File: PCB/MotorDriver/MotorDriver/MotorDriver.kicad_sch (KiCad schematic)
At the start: 74 parts, among them J13 JST-XH, J14 JST-XH, J2 JST-XH, J3 XT30PW-M, J5 JST-XH, J6 JST-XH, J7 JST-XH, J8 JST-XH, J9 JST-XH, Q10 NMOS, Q3 TJ60S04M3L, SW1 SW_Push, SW2 SW_DPST_x2, U1 Pico, U15 AZ1117CH-3.3TR, U3 TCA9548APWR

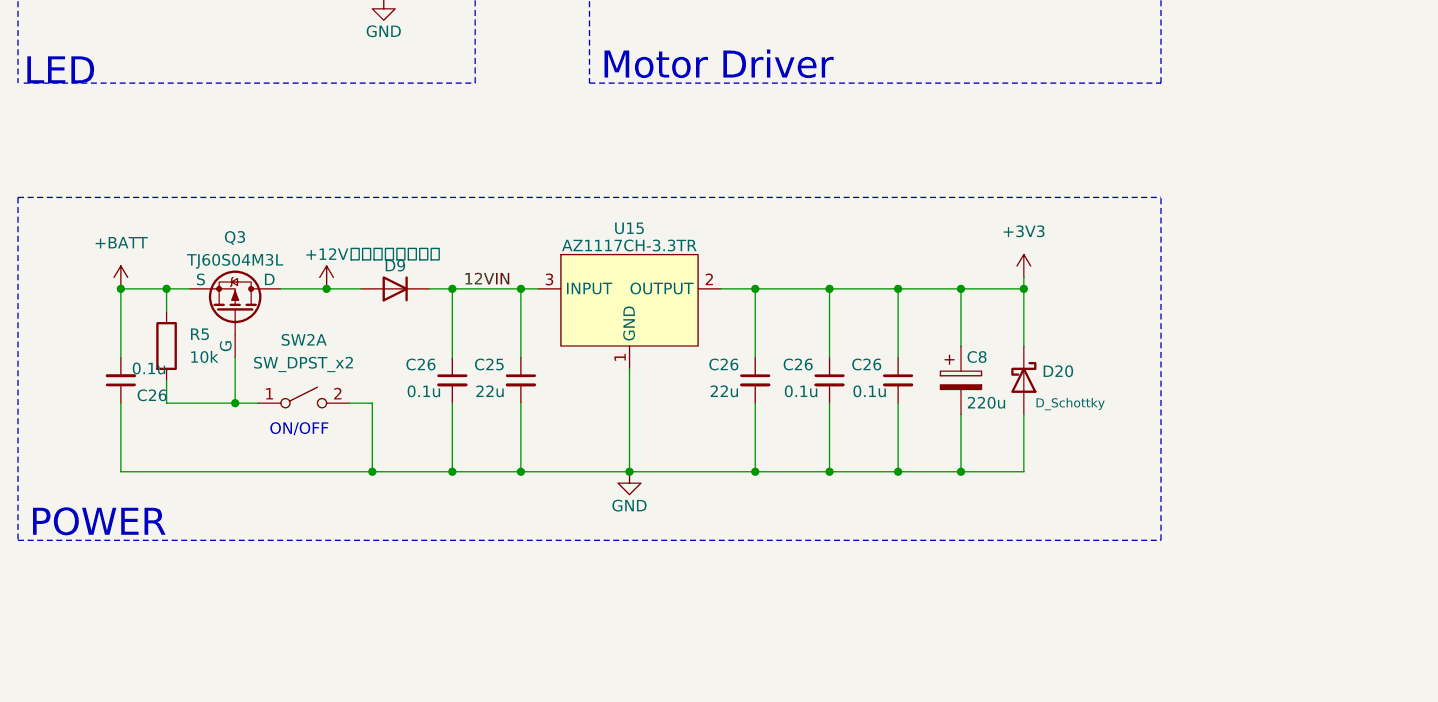
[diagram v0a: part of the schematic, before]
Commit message: ✨基板をサージに強くした
- TVSをサージ発生源に近くした
- 12Vツェナーダイオードをレギュレータの近くに取り付けた
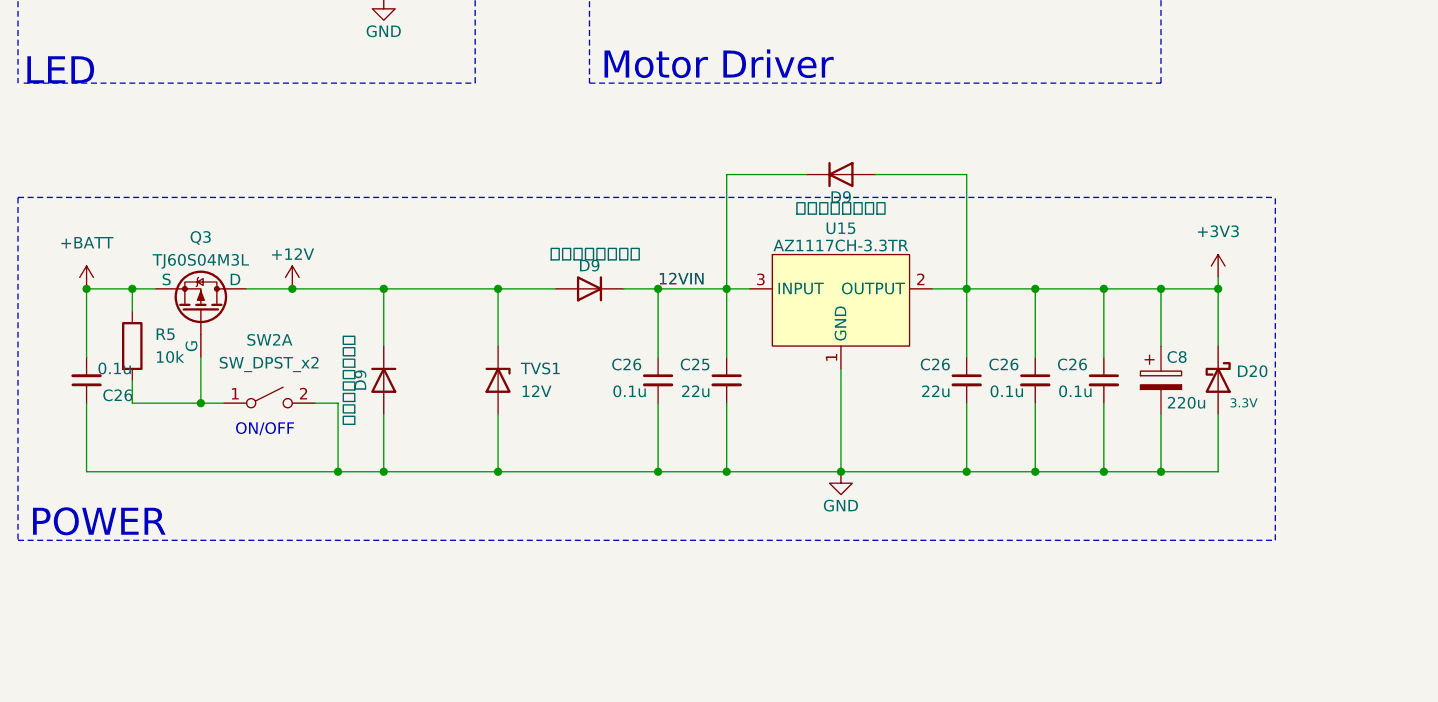
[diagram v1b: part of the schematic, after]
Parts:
- added D9 (x2): ＧＳ１０１０ＦＬ, Diode_SMD:D_SOD-123F, symbol Device:D
- added TVS1: 12V, Diode_SMD:D_SMB, symbol Device:D_Zener
- D20: value D_Schottky -> 3.3V
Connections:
- net +12V: now also D9.1 (K), TVS1.1 (K)
- net +3V3: now also D9.2 (A)
- net 12VIN: now also D9.1 (K)
- net GND: now also D9.2 (A), TVS1.2 (A)
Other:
- moved on the sheet: C25, C26, C8, D20, D9, Q3, R5, SW2A, U15
